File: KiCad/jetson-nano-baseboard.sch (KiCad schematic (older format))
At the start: 0 parts

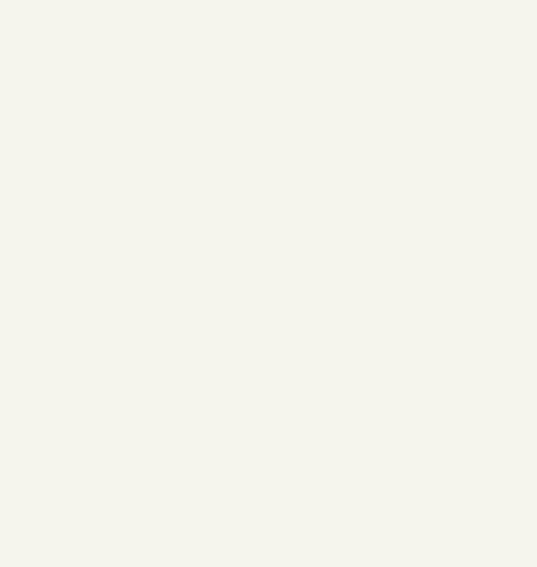
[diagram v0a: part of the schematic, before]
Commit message: Add logo and clean up libraries
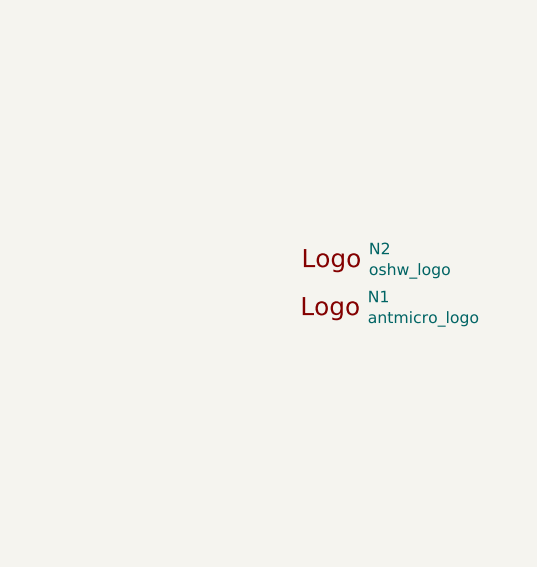
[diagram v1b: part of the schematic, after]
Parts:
- added N1: antmicro_logo, jetson-nano-baseboard-footprints:antmicro-logo_scaled_15mm, symbol jetson-nano-baseboard:antmicro_logo
- added N2: oshw_logo, jetson-nano-baseboard-footprints:oshw-logo, symbol jetson-nano-baseboard:oshw_logo
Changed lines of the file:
@@
 F1 "som.sch" 50
 $EndSheet
+$Comp
+L jetson-nano-baseboard:antmicro_logo N1
+U 1 1 60BDCA6D
+P 15100 9725
+F 0 "N1" H 15314 9818 50  0000 L CNN
+F 1 "antmicro_logo" H 15314 9727 50  0000 L CNN
+F 2 "jetson-nano-baseboard-footprints:antmicro-logo_scaled_15mm" H 15000 9975 50  0001 C CNN
+F 3 "" H 15100 10075 50  0001 C CNN
+	1    15100 9725
+	1    0    0    -1
+$EndComp
+$Comp
+L jetson-nano-baseboard:oshw_logo N2
+U 1 1 60BDCE33
+P 15125 9425
+F 0 "N2" H 15319 9428 50  0000 L CNN
+F 1 "oshw_logo" H 15319 9337 50  0000 L CNN
+F 2 "jetson-nano-baseboard-footprints:oshw-logo" H 15145 9185 50  0001 C CNN
+F 3 "" H 15125 9425 50  0001 C CNN
+	1    15125 9425
+	1    0    0    -1
+$EndComp
 $EndSCHEMATC

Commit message: Add CRC logo
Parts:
- added N?: crc_logo, jetson-nano-baseboard-footprints:CRC_logo_15mm, symbol jetson-nano-baseboard:crc_logo
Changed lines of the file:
@@
+	1    0    0    -1
+$EndComp
+$Comp
+L jetson-nano-baseboard:crc_logo N?
+U 1 1 60CB08FE
+P 15125 9200
+F 0 "N?" H 15319 9203 50  0000 L CNN
+F 1 "crc_logo" H 15319 9112 50  0000 L CNN
+F 2 "jetson-nano-baseboard-footprints:CRC_logo_15mm" H 15145 8960 50  0001 C CNN
+F 3 "" H 15125 9200 50  0001 C CNN
+	1    15125 9200
 	1    0    0    -1
 $EndComp
